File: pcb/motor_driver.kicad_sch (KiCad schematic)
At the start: 0 parts

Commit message: Created DRV8353S and added Driver
Also created Symbol, Footprint, and Models libraries
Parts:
- added U2: DRV8353S, symbol Symbols:DRV8353S
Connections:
- new net GHA: U2.6 (GHA)
- new net GHB: U2.15 (GHB)
- new net GHC: U2.16 (GHC)
- new net GLA: U2.8 (GLA)
- new net GLB: U2.13 (GLB)
- new net GLC: U2.18 (GLC)
- new net SHA: U2.7 (SHA)
- new net SHB: U2.14 (SHB)
- new net SHC: U2.17 (SHC)
- new net SNA: U2.10 (SNA)
- new net SNB: U2.11 (SNB)
- new net SNC: U2.20 (SNC)
- new net SPA: U2.9 (SPA)
- new net SPB: U2.12 (SPB)
- new net SPC: U2.19 (SPC)

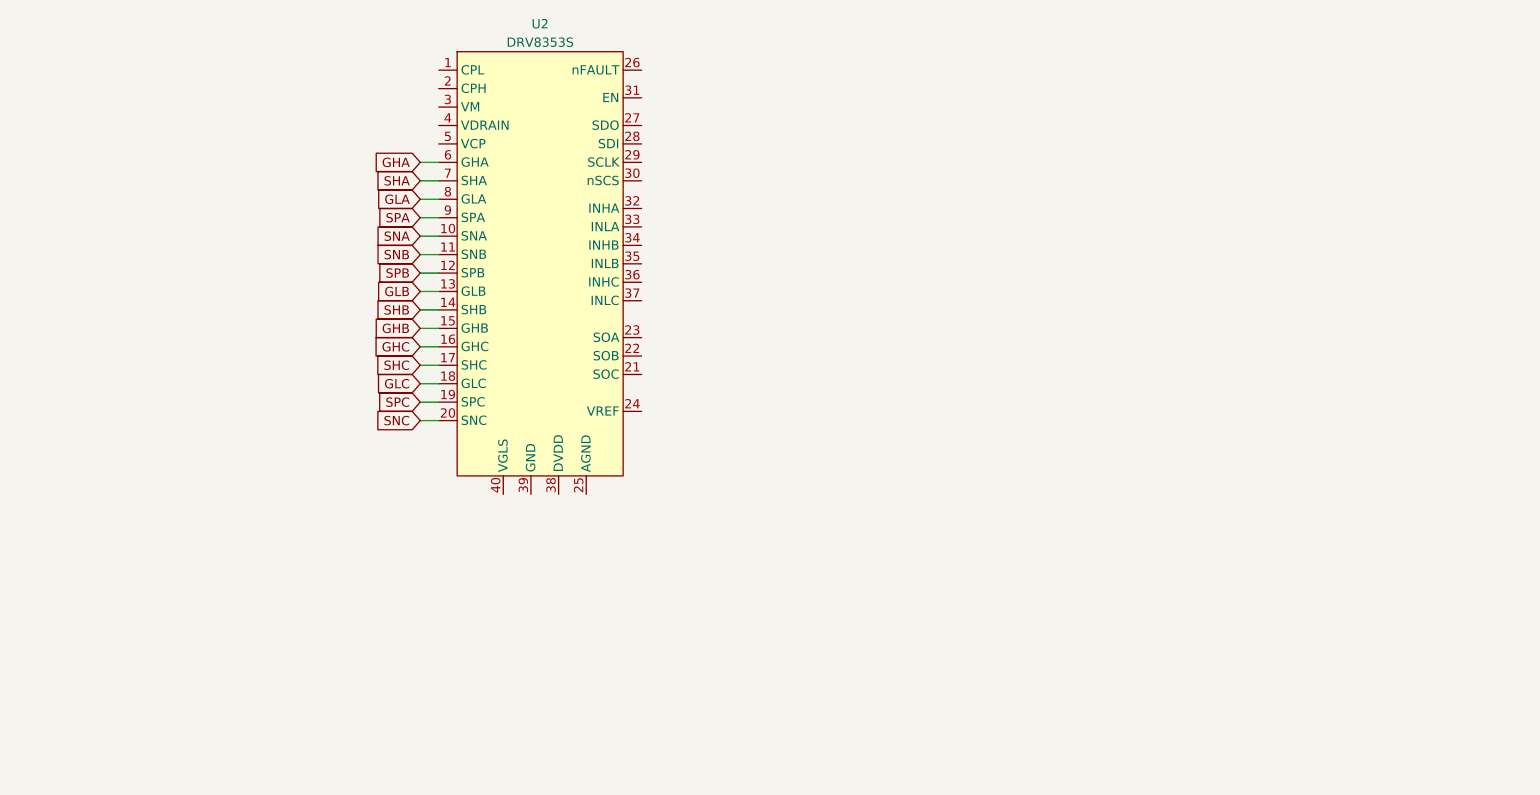
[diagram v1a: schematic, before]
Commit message: Created DRV8353S and added Driver
Also created Symbol, Footprint, and Models libraries
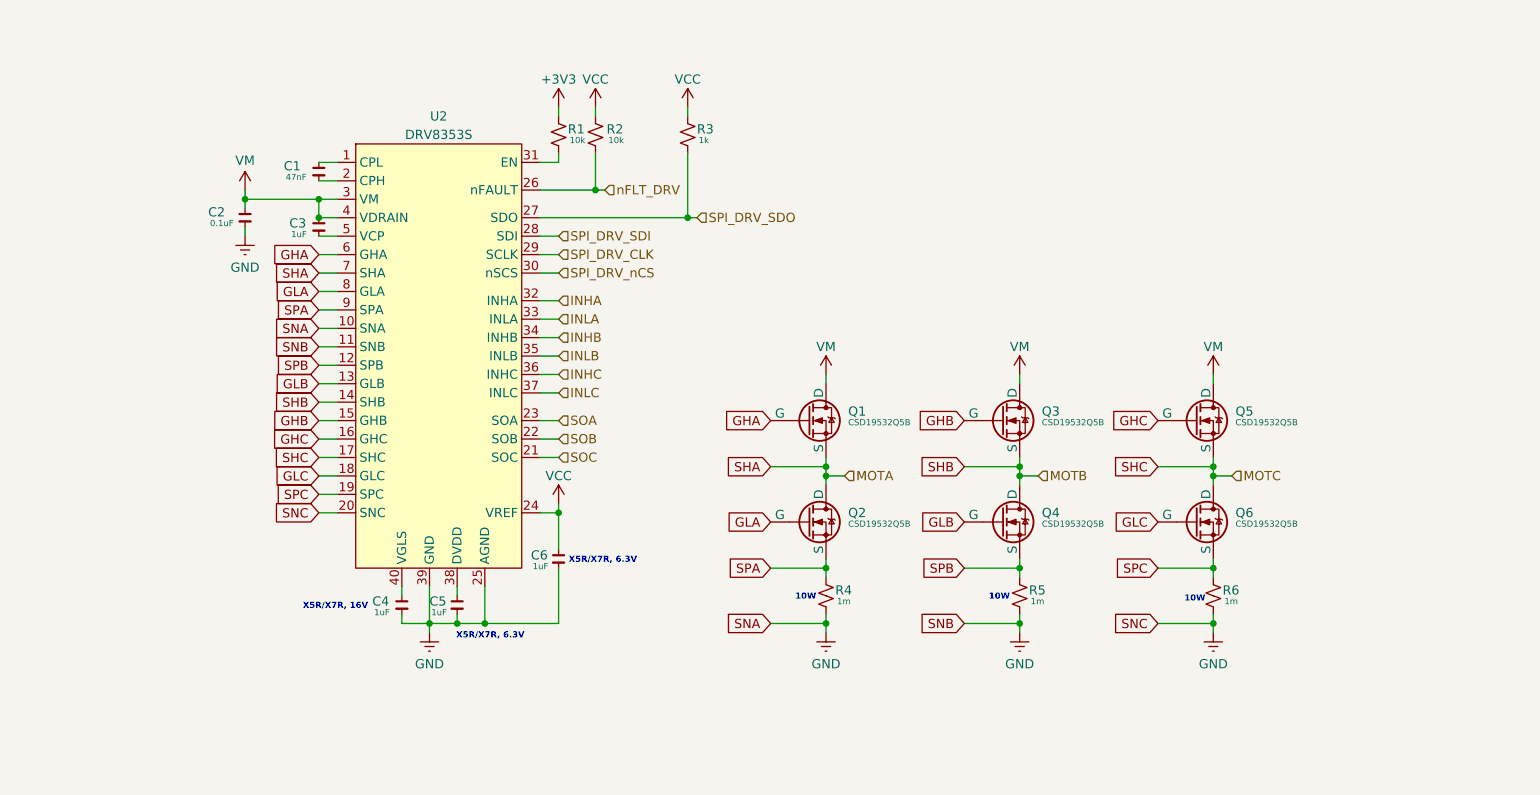
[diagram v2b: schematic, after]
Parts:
- added C1: 47nF, Capacitor_SMD:C_0402_1005Metric_Pad0.74x0.62mm_HandSolder, symbol Device:C_Small
- added C2: 0.1uF, Capacitor_SMD:C_0402_1005Metric_Pad0.74x0.62mm_HandSolder, symbol Device:C_Small
- added C3, C4, C5, C6: 1uF, Capacitor_SMD:C_0402_1005Metric_Pad0.74x0.62mm_HandSolder, symbol Device:C_Small
- added Q1, Q2, Q3, Q4, Q5, Q6: CSD19532Q5B, symbol Simulation_SPICE:NMOS
- added R1, R2: 10k, symbol Device:R_Small_US
- added R3: 1k, symbol Device:R_Small_US
- added R4, R5, R6: 1m, symbol Device:R_Small_US
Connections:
- net SNA is gone; now on net GND: U2.10 (SNA)
- net SNB is gone; now on net GND: U2.11 (SNB)
- net SNC is gone; now on net GND: U2.20 (SNC)
- net GHA: now also Q1.2 (G)
- net GHB: now also Q3.2 (G)
- net GHC: now also Q5.2 (G)
- net GLA: now also Q2.2 (G)
- net GLB: now also Q4.2 (G)
- net GLC: now also Q6.2 (G)
- net SHA: now also Q1.3 (S), Q2.1 (D)
- net SHB: now also Q3.3 (S), Q4.1 (D)
- net SHC: now also Q5.3 (S), Q6.1 (D)
- net SPA: now also Q2.3 (S), R4.1
- net SPB: now also Q4.3 (S), R5.1
- net SPC: now also Q6.3 (S), R6.1
- net at U2.1 (CPL): now also C1.1
- net at U2.2 (CPH): now also C1.2
- net SOC: now reaches U2.21 (SOC)
- net SOB: now reaches U2.22 (SOB)
- net SOA: now reaches U2.23 (SOA)
- net VCC: now reaches U2.24 (VREF)
- net VCC: now also C6.1, R2.1, R3.1
- net GND: now reaches U2.25 (AGND)
- net GND: now also U2.39 (GND), C2.2, C4.2, C5.2, C6.2, R4.2, R5.2, R6.2
- net nFLT_DRV: now reaches U2.26 (nFAULT)
- net nFLT_DRV: now also R2.2
- net SPI_DRV_SDO: now reaches U2.27 (SDO)
- net SPI_DRV_SDO: now also R3.2
- net SPI_DRV_SDI: now reaches U2.28 (SDI)
- net SPI_DRV_CLK: now reaches U2.29 (SCLK)
- net VM: now reaches U2.3 (VM)
- net VM: now also U2.4 (VDRAIN), C2.1, C3.1, Q1.1 (D), Q3.1 (D), Q5.1 (D)
- net SPI_DRV_nCS: now reaches U2.30 (nSCS)
- net at U2.31 (EN): now also R1.2
- net INHA: now reaches U2.32 (INHA)
- net INLA: now reaches U2.33 (INLA)
- net INHB: now reaches U2.34 (INHB)
- net INLB: now reaches U2.35 (INLB)
- net INHC: now reaches U2.36 (INHC)
- net INLC: now reaches U2.37 (INLC)
- net at U2.38 (DVDD): now also C5.1
- net at U2.40 (VGLS): now also C4.1
- net at U2.5 (VCP): now also C3.2
- new net +3V3: R1.1
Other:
- note added: "10W"
- note added: "X5R/X7R, 16V"
- note added: "X5R/X7R, 6.3V"
- moved on the sheet: U2

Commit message: Cleaned up Driver and added decaps
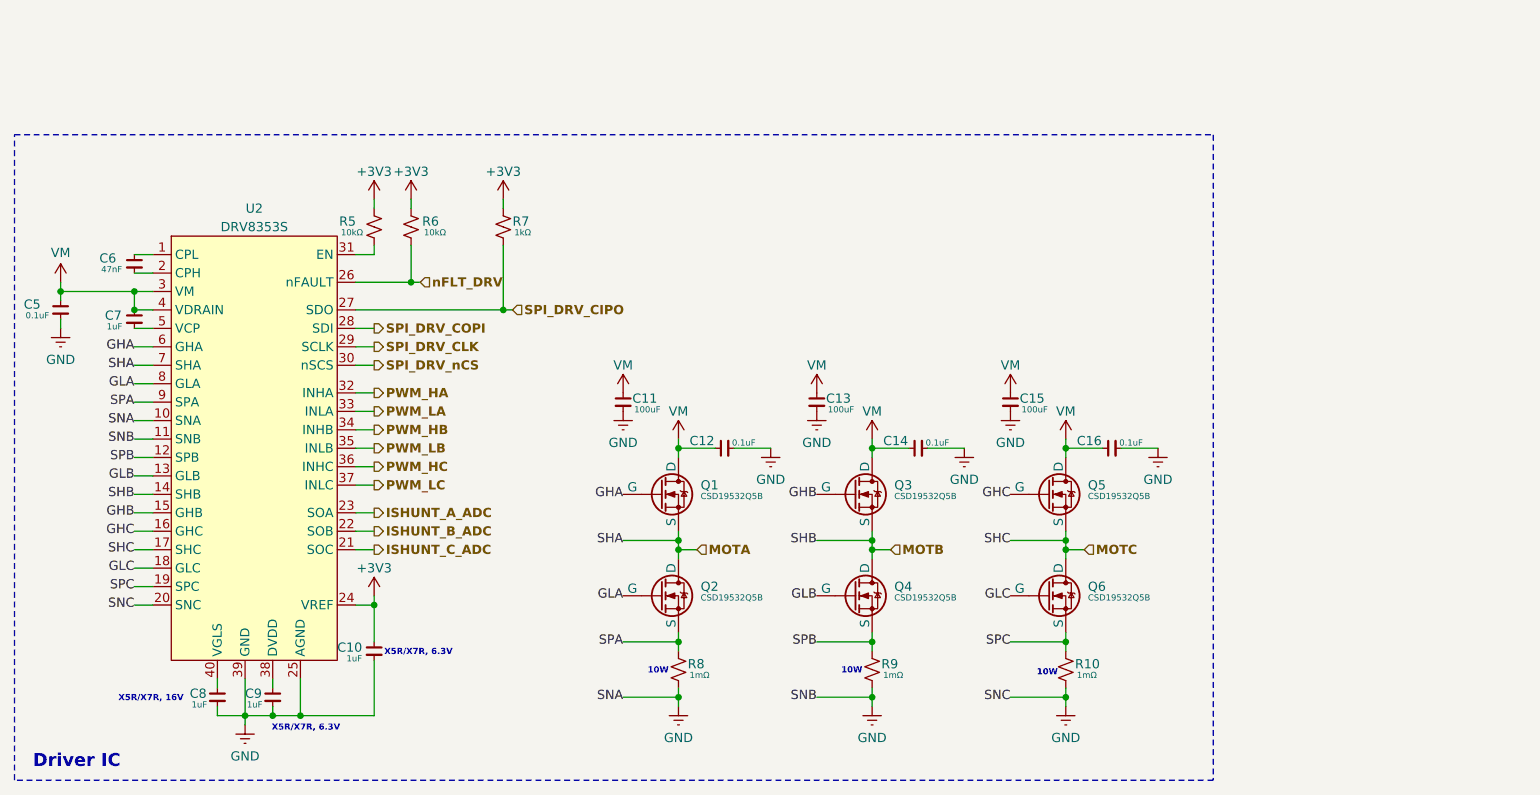
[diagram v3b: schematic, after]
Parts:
- removed C1: 47nF, Capacitor_SMD:C_0402_1005Metric_Pad0.74x0.62mm_HandSolder, symbol Device:C_Small
- removed C2: 0.1uF, Capacitor_SMD:C_0402_1005Metric_Pad0.74x0.62mm_HandSolder, symbol Device:C_Small
- removed C4: 1uF, Capacitor_SMD:C_0402_1005Metric_Pad0.74x0.62mm_HandSolder, symbol Device:C_Small
- added C10, C8, C9: 1uF, Capacitor_SMD:C_0402_1005Metric_Pad0.74x0.62mm_HandSolder, symbol Device:C_Small
- added C11, C13, C15: 100uF, Capacitor_SMD:C_0402_1005Metric_Pad0.74x0.62mm_HandSolder, symbol Device:C_Small
- added C12, C14, C16: 0.1uF, Capacitor_SMD:C_0402_1005Metric_Pad0.74x0.62mm_HandSolder, symbol Device:C_Small
- C5: value 1uF -> 0.1uF
- C6: value 1uF -> 47nF
- R10: renamed from R6; value 1m -> 1mΩ
- R5: renamed from R1; value 10k -> 10kΩ
- R6: renamed from R2; value 10k -> 10kΩ
- R7: renamed from R3; value 1k -> 1kΩ
- R8: renamed from R4; value 1m -> 1mΩ
- R9: renamed from R5; value 1m -> 1mΩ
- renumbered C3 to C7
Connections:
- net +3V3: now also R6.1, R7.1, U2.24 (VREF), C10.1
- net GND: now also C10.2, C11.2, C12.2, C13.2, C14.2, C15.2, C16.2, C8.2, C9.2; no longer C6.2
- net VM: now also C5.1, C11.1, C12.1, C13.1, C14.1, C15.1, C16.1
- net at U2.38 (DVDD): now also C9.1; no longer C5.1
- net at U2.1 (CPL): now also C6.1
- net at U2.2 (CPH): now also C6.2
- net at U2.40 (VGLS): now also C8.1
- net INHA renamed PWM_HA
- net INHB renamed PWM_HB
- net INHC renamed PWM_HC
- net INLA renamed PWM_LA
- net INLB renamed PWM_LB
- net INLC renamed PWM_LC
- net SHA renamed MOTA
- net SHB renamed MOTB
- net SHC renamed MOTC
- net SOA renamed ISHUNT_A_ADC
- net SOB renamed ISHUNT_B_ADC
- net SOC renamed ISHUNT_C_ADC
- net SPI_DRV_SDI renamed SPI_DRV_COPI
- net SPI_DRV_SDO renamed SPI_DRV_CIPO
- removed net VCC: C6.1, R6.1, R7.1, U2.24 (VREF)
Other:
- note added: "Driver IC"
- moved on the sheet: C7, Q1, Q2, Q3, Q4, Q5, Q6, R10, R5, R6, R7, R8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

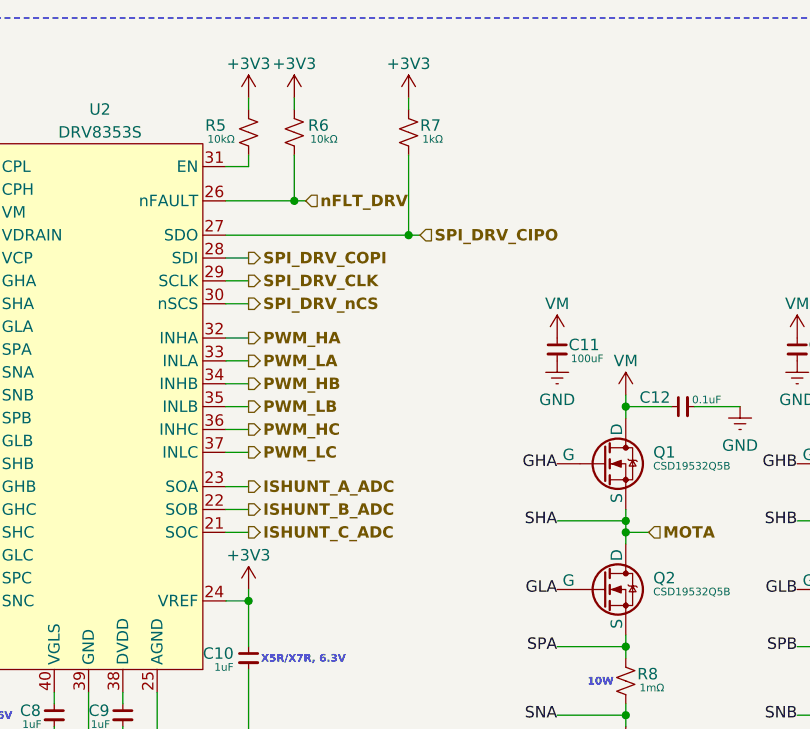
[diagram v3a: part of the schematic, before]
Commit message: Completed Initial Power Draft for Review, and Updated Flags
Included notes for review
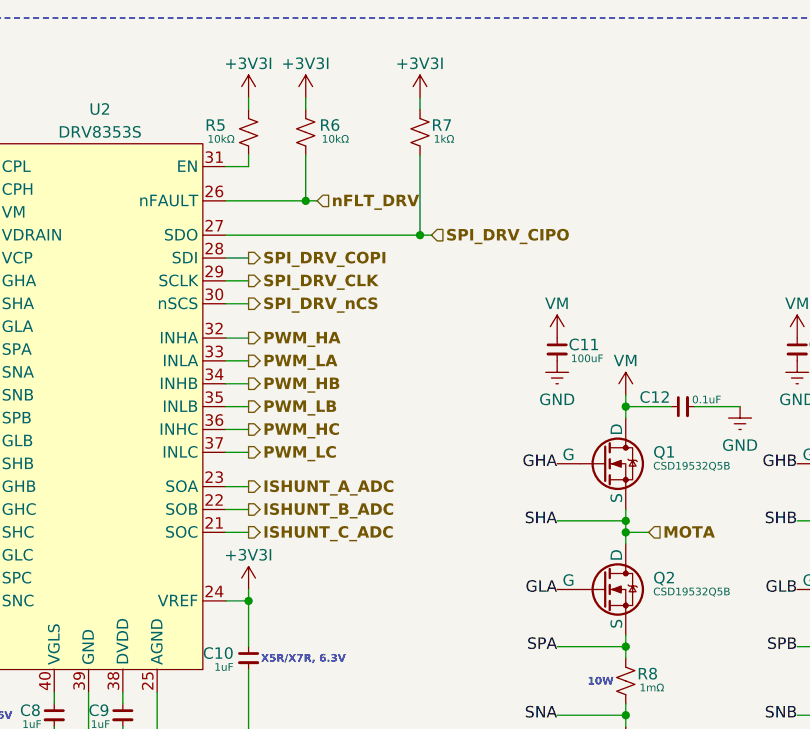
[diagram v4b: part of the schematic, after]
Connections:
- net +3V3 renamed +3V3I
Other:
- moved on the sheet: R6, R7
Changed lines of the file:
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@@
 	)
 	(junction
-		(at 118.11 71.12)
+		(at 95.25 130.81)
 		(diameter 0)
 		(color 0 0 0 0)
 	)
 	(junction
-		(at 95.25 130.81)
+		(at 132.08 74.93)
 		(diameter 0)
 		(color 0 0 0 0)
@@
 	)
 	(junction
-		(at 181.61 128.27)
+		(at 119.38 71.12)
 		(diameter 0)
 		(color 0 0 0 0)
 	)
 	(junction
-		(at 181.61 107.95)
+		(at 181.61 128.27)
 		(diameter 0)
 		(color 0 0 0 0)
 	)
 	(junction
-		(at 80.01 74.93)
+		(at 181.61 107.95)
 		(diameter 0)
 		(color 0 0 0 0)
 	)
 	(junction
-		(at 208.28 128.27)
+		(at 80.01 74.93)
 		(diameter 0)
 		(color 0 0 0 0)
 	)
 	(junction
-		(at 130.81 74.93)
+		(at 208.28 128.27)
 		(diameter 0)
 		(color 0 0 0 0)
@@
 	(wire
 		(pts
-			(xy 110.49 71.12) (xy 118.11 71.12)
+			(xy 110.49 71.12) (xy 119.38 71.12)
 		)
 		(stroke
@@
 	(wire
 		(pts
-			(xy 118.11 66.04) (xy 118.11 71.12)
+			(xy 119.38 66.04) (xy 119.38 71.12)
 		)
 		(stroke
@@
 	(wire
 		(pts
-			(xy 110.49 74.93) (xy 130.81 74.93)
+			(xy 110.49 74.93) (xy 132.08 74.93)
 		)
 		(stroke
@@
 	(wire
 		(pts
-			(xy 130.81 74.93) (xy 132.08 74.93)
-		)
-		(stroke
-			(width 0)
-			(type default)
-		)
-	)
-	(wire
-		(pts
 			(xy 181.61 93.98) (xy 181.61 95.25)
 		)
@@
 	(wire
 		(pts
-			(xy 130.81 66.04) (xy 130.81 74.93)
+			(xy 132.08 66.04) (xy 132.08 74.93)
 		)
 		(stroke
@@
 	(wire
 		(pts
+			(xy 132.08 74.93) (xy 133.35 74.93)
+		)
+		(stroke
+			(width 0)
+			(type default)
+		)
+	)
+	(wire
+		(pts
 			(xy 154.94 128.27) (xy 154.94 127)
 		)
@@
 	(wire
 		(pts
-			(xy 119.38 71.12) (xy 118.11 71.12)
+			(xy 120.65 71.12) (xy 119.38 71.12)
 		)
 		(stroke
@@
 	(wire
 		(pts
-			(xy 118.11 59.69) (xy 118.11 60.96)
+			(xy 119.38 59.69) (xy 119.38 60.96)
 		)
 		(stroke
@@
 	(wire
 		(pts
-			(xy 130.81 59.69) (xy 130.81 60.96)
+			(xy 132.08 59.69) (xy 132.08 60.96)
 		)
 		(stroke
@@
 	(hierarchical_label "nFLT_DRV"
 		(shape input)
-		(at 119.38 71.12 0)
+		(at 120.65 71.12 0)
 		(effects
 			(font
@@
 	(hierarchical_label "SPI_DRV_CIPO"
 		(shape input)
-		(at 132.08 74.93 0)
+		(at 133.35 74.93 0)
 		(effects
 			(font
@@
 	(symbol
 		(lib_id "power:VCC")
-		(at 130.81 59.69 0)
+		(at 132.08 59.69 0)
 		(unit 1)
 		(exclude_from_sim no)
@@
 		(dnp no)
 		(property "Reference" "#PWR017"
-			(at 130.81 63.5 0)
+			(at 132.08 63.5 0)
 			(effects
 				(font
@@
 			)
 		)
-		(property "Value" "+3V3"
-			(at 130.81 55.88 0)
+		(property "Value" "+3V3I"
+			(at 132.08 55.88 0)
 			(effects
 				(font
@@
 		)
 		(property "Footprint" ""
-			(at 130.81 59.69 0)
+			(at 132.08 59.69 0)
 			(effects
 				(font
@@
 		)
 		(property "Datasheet" ""
-			(at 130.81 59.69 0)
+			(at 132.08 59.69 0)
 			(effects
 				(font
@@
 		)
 		(property "Description" "Power symbol creates a global label with name \"VCC\""
-			(at 130.81 59.69 0)
+			(at 132.08 59.69 0)
 			(effects
 				(font
@@
 			)
 		)
-		(property "Value" "+3V3"
+		(property "Value" "+3V3I"
 			(at 113.03 110.49 0)
 			(effects
@@
 	(symbol
 		(lib_id "power:VCC")
-		(at 118.11 59.69 0)
+		(at 119.38 59.69 0)
 		(unit 1)
 		(exclude_from_sim no)
@@
 		(dnp no)
 		(property "Reference" "#PWR016"
-			(at 118.11 63.5 0)
+			(at 119.38 63.5 0)
 			(effects
 				(font
@@
 			)
 		)
-		(property "Value" "+3V3"
-			(at 118.11 55.88 0)
+		(property "Value" "+3V3I"
+			(at 119.38 55.88 0)
 			(effects
 				(font
@@
 		)
 		(property "Footprint" ""
-			(at 118.11 59.69 0)
+			(at 119.38 59.69 0)
 			(effects
 				(font
@@
 		)
 		(property "Datasheet" ""
-			(at 118.11 59.69 0)
+			(at 119.38 59.69 0)
 			(effects
 				(font
@@
 		)
 		(property "Description" "Power symbol creates a global label with name \"VCC\""
-			(at 118.11 59.69 0)
+			(at 119.38 59.69 0)
 			(effects
 				(font
@@
 			)
 		)
-		(property "Value" "+3V3"
+		(property "Value" "+3V3I"
 			(at 113.03 55.88 0)
 			(effects
@@
 	(symbol
 		(lib_id "Device:R_Small_US")
-		(at 130.81 63.5 0)
+		(at 132.08 63.5 0)
 		(unit 1)
 		(exclude_from_sim no)
@@
 		(dnp no)
 		(property "Reference" "R7"
-			(at 132.08 62.738 0)
+			(at 133.35 62.738 0)
 			(effects
 				(font
@@
 		)
 		(property "Value" "1kΩ"
-			(at 132.334 64.262 0)
+			(at 133.604 64.262 0)
 			(effects
 				(font
@@
 		)
 		(property "Footprint" ""
-			(at 130.81 63.5 0)
+			(at 132.08 63.5 0)
 			(effects
 				(font
@@
 		)
 		(property "Datasheet" "~"
-			(at 130.81 63.5 0)
+			(at 132.08 63.5 0)
 			(effects
 				(font
@@
 		)
 		(property "Description" "Resistor, small US symbol"
-			(at 130.81 63.5 0)
+			(at 132.08 63.5 0)
 			(effects
 				(font
@@
 	(symbol
 		(lib_id "Device:R_Small_US")
-		(at 118.11 63.5 0)
+		(at 119.38 63.5 0)
 		(unit 1)
 		(exclude_from_sim no)
@@
 		(dnp no)
 		(property "Reference" "R6"
-			(at 119.634 62.738 0)
+			(at 120.904 62.738 0)
 			(effects
 				(font
@@
 		)
 		(property "Value" "10kΩ"
-			(at 119.888 64.262 0)
+			(at 121.158 64.262 0)
 			(effects
 				(font
@@
 		)
 		(property "Footprint" ""
-			(at 118.11 63.5 0)
+			(at 119.38 63.5 0)
 			(effects
 				(font
@@
 		)
 		(property "Datasheet" "~"
-			(at 118.11 63.5 0)
+			(at 119.38 63.5 0)
 			(effects
 				(font
@@
 		)
 		(property "Description" "Resistor, small US symbol"
-			(at 118.11 63.5 0)
+			(at 119.38 63.5 0)
 			(effects
 				(font
